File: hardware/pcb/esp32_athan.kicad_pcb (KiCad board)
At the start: 2 copper layers, 59.6 x 50 mm, 39 parts, among them J1 USB_C_Receptacle_PowerOnly_6P, J2 Barrel_Jack, J3 Speaker, J5 Relay, J6 PROG, U1 ESP32-S3-WROOM-1-N16R8, U2 SKQUAAA010, U3 AMS1117-3.3, U4 MAX98357A

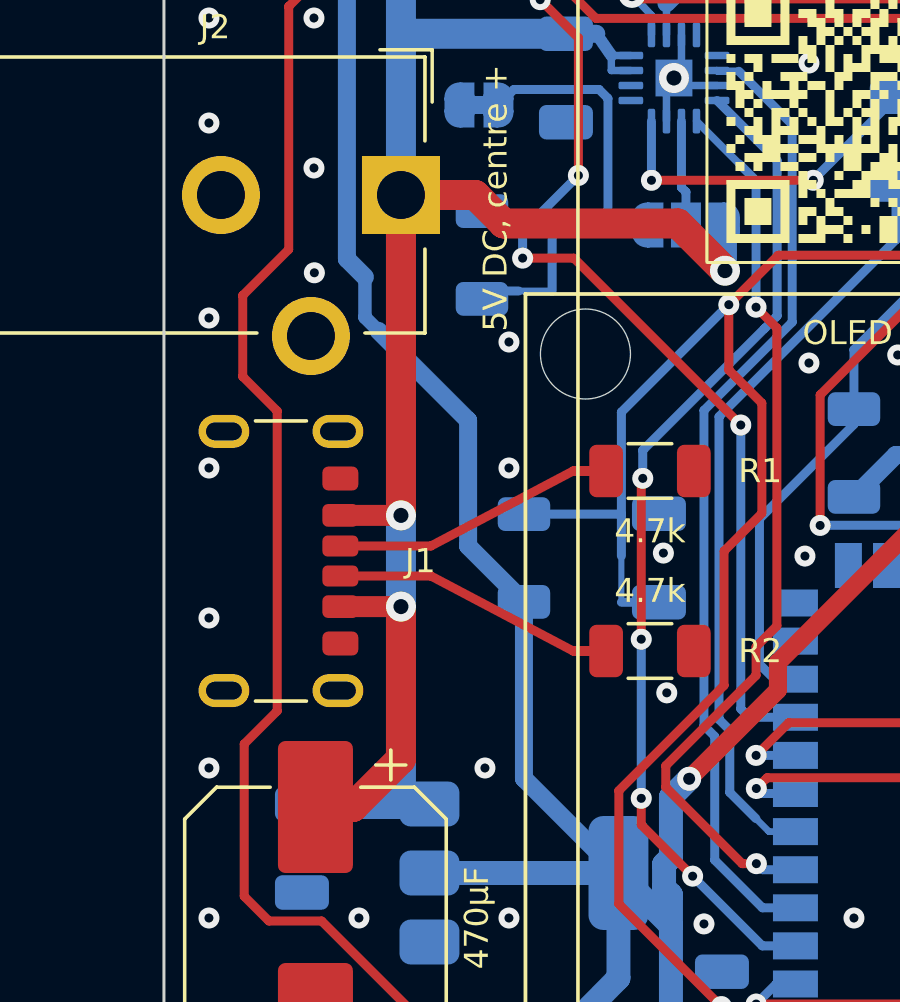
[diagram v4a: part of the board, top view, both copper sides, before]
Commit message: USB-C on either side, switch named by its real part, STEP out of the repo
Board
- J1 has a new footprint, USB_C_Receptacle_GCT_USB4125_6P_BothSides
  (project library): KiCad's GCT USB4125 with its six pads also on the
  back, the four shell legs in shared holes. The receptacle can be
  soldered on the front by hand or placed on the back by JLCPCB. Flipped
  onto the back, its A and B pins land on each other's pads: CC1 and CC2
  swap (each has its own 4.7 kΩ), VBUS and GND stay on their nets.
- Copper at J1 rearranged for the back pads: the two +5V vias moved
  1.1 mm right, VBUS pads on both sides tracked to them, and two vias take
  the back CC pads to the front lines to R1 and R2.
- A +3V3 track on the back near U4 is now two 0.6 mm segments.
- U2 is named for the switch it is: "5-way switch (SKQUCAA010 type)",
  a 10 x 10 mm through-hole 5-way switch with a centre push (Alps
  SKQUCAA010 or a copy). Its description warns that Alps' SKQUAAA010,
  which fits the same holes, has no centre push. SnapEDA's shop links
  for SKQUAAA010 are removed; the pins and footprint are unchanged.
- Checks: DRC 0 errors, 0 unconnected, schematic and board match, ERC 0
  errors.

JLCPCB files
- jlcpcb_assembly.py places a part whose footprint has pads on both
  sides on the side the selection file names ("sides", the back by
  default), as the same part flipped over. --verify checks it against
  JLCPCB's footprint like every other part: J1 on the back fits within
  0.075 mm.
- jlcpcb_select.py draws J1 on both sides (dotted blue where it is not
  fitted); a click on the other side moves it there. The choice is saved
  in jlcpcb_selection.json, now J1 on the back.
- generate_fab_files.sh notes J1's side in fab_files/README.md.
- J1 joins the back-only order: three extended parts there (U1, U4, J1).
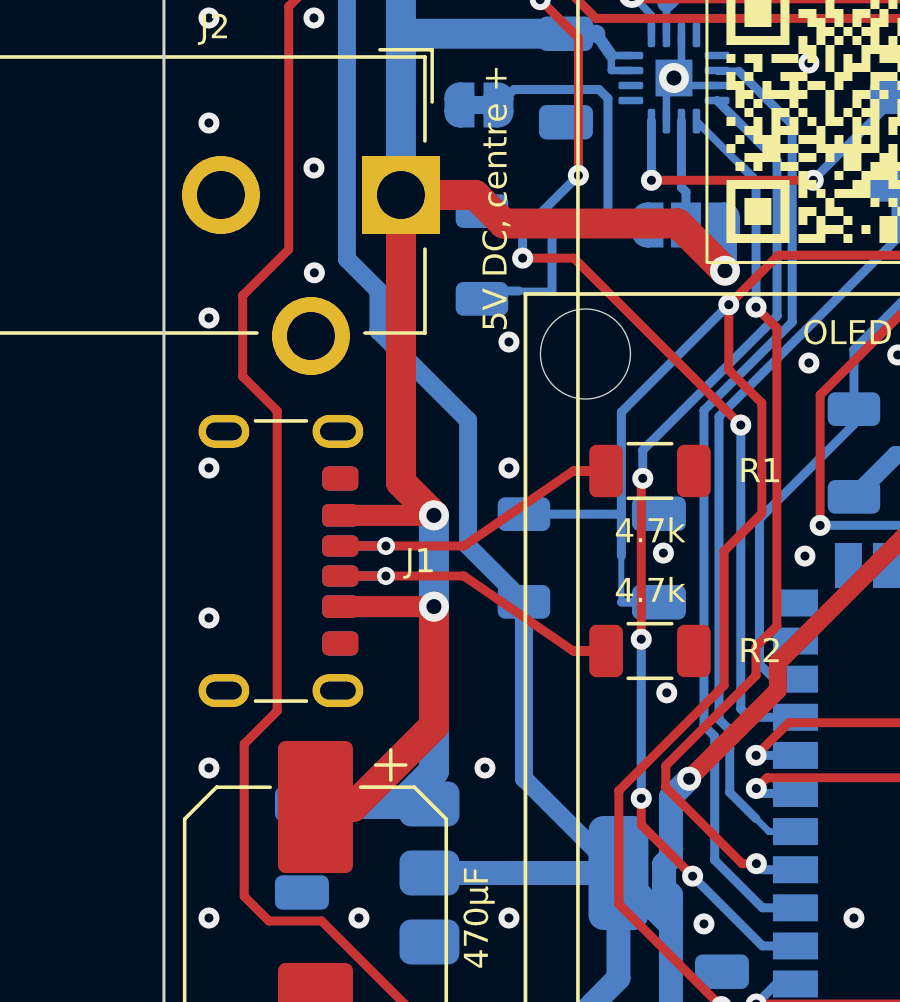
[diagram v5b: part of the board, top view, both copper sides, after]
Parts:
- J1: footprint Connector_USB:USB_C_Receptacle_GCT_USB4125-xx-x_6P_TopMnt_Horizontal -> Library:USB_C_Receptacle_GCT_USB4125_6P_BothSides
- U2: value SKQUAAA010 -> 5-way switch (SKQUCAA010 type)
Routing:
- net +5V: track 67.2 -> 77.1 mm
- net Net-(J1-CC2): track 10.6 -> 12.3 mm, vias 0 -> 1
- net Net-(J1-CC1): track 10.6 -> 12.3 mm, vias 0 -> 1
